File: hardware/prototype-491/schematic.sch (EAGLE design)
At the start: 27 parts, among them IC1 LM2576T, IC2 LM2576T, Q1 220mA/50V/3.5Ω, Q2 220mA/50V/3.5Ω

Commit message: CAM files for PCB
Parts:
- J1: value (none) -> OBD_CONN
- J2: value (none) -> SUPPLY
- JP1: value (none) -> ADXL345
- JP8: value DNP -> UART_CONN
- L1, L2: value (none) -> 100uH
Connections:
- removed net VCC: C2.+, IC2.VIN, J2.1
- net VBAT: now also C2.+, IC2.VIN, J2.1
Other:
- note added: "ECE 491 Group 7 Vehicle Immobilizer Prototype Board Schematic"
- note removed: "ADXL345 Breakout Board"
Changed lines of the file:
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@@
 <clearance class="0" value="0.3048"/>
+</class>
+<class number="1" name="power" width="1.27" drill="0.508">
+<clearance class="1" value="0.508"/>
 </class>
 </classes>
 <parts>
-<part name="JP1" library="microbuilder" deviceset="HEADER-1X9" device="70MIL"/>
+<part name="JP1" library="microbuilder" deviceset="HEADER-1X9" device="70MIL" value="ADXL345"/>
 <part name="U$6" library="microbuilder" deviceset="GND" device=""/>
 <part name="P+1" library="supply1" library_urn="urn:adsk.eagle:library:371" deviceset="+5V" device=""/>
@@
 <part name="GND4" library="supply1" library_urn="urn:adsk.eagle:library:371" deviceset="GND" device=""/>
 <part name="P+2" library="supply1" library_urn="urn:adsk.eagle:library:371" deviceset="+5V" device=""/>
-<part name="JP8" library="SparkFun" deviceset="FTDI_BASIC" device="PTH" value="DNP"/>
+<part name="JP8" library="SparkFun" deviceset="FTDI_BASIC" device="PTH" value="UART_CONN"/>
 <part name="GND32" library="SparkFun" deviceset="GND" device=""/>
 <part name="MCU" library="RPI-Zero" deviceset="RPI-ZERO" device=""/>
@@
 <part name="IC2" library="v-reg-3" deviceset="LM2576" device="T"/>
 <part name="D1" library="1N5822" deviceset="1N5822" device=""/>
-<part name="L1" library="PowerMagnetics" deviceset="WE-TI_1014" device="" technology="_7447480101"/>
+<part name="L1" library="PowerMagnetics" deviceset="WE-TI_1014" device="" technology="_7447480101" value="100uH"/>
 <part name="C1" library="cap-pan40" deviceset="C-PR" device="-3,5X8" value="1000uF"/>
 <part name="C2" library="cap-pan40" deviceset="C-PR" device="-3,5X8" value="100uF"/>
@@
 <part name="IC1" library="v-reg-3" deviceset="LM2576" device="T"/>
 <part name="D2" library="1N5822" deviceset="1N5822" device=""/>
-<part name="L2" library="PowerMagnetics" deviceset="WE-TI_1014" device="" technology="_7447480101"/>
+<part name="L2" library="PowerMagnetics" deviceset="WE-TI_1014" device="" technology="_7447480101" value="100uH"/>
 <part name="C3" library="cap-pan40" deviceset="C-PR" device="-3,5X8" value="1000uF"/>
 <part name="C4" library="cap-pan40" deviceset="C-PR" device="-3,5X8" value="100uF"/>
 <part name="P+7" library="supply1" library_urn="urn:adsk.eagle:library:371" deviceset="+5V" device=""/>
-<part name="SUPPLY1" library="SparkFun-PowerSymbols" deviceset="3.3V" device=""/>
 <part name="SUPPLY4" library="SparkFun-PowerSymbols" deviceset="3.3V" device=""/>
-<part name="FRAME1" library="frames" library_urn="urn:adsk.eagle:library:229" deviceset="FRAME_A_L" device=""/>
-<part name="J1" library="SparkFun-Connectors" deviceset="CONN_08" device="&quot;"/>
-<part name="J2" library="SparkFun-Connectors" deviceset="CONN_02" device="POLAR"/>
+<part name="FRAME1" library="frames" library_urn="urn:adsk.eagle:library:229" deviceset="FRAME_A_L" device="" value="frame"/>
+<part name="J1" library="SparkFun-Connectors" deviceset="CONN_08" device="&quot;" value="OBD_CONN"/>
+<part name="J2" library="SparkFun-Connectors" deviceset="CONN_02" device="POLAR" value="SUPPLY"/>
 <part name="P+8" library="SparkFun" deviceset="VCC" device="" value="VBAT"/>
 <part name="GND9" library="SparkFun" deviceset="GND" device=""/>
@@
 <sheet>
 <plain>
-<text x="294.64" y="71.12" size="1.778" layer="91" rot="R90">ADXL345 Breakout Board
-</text>
+<text x="231.14" y="53.34" size="2.1844" layer="94">ECE 491 Group 7 Vehicle Immobilizer Prototype Board Schematic</text>
 </plain>
 <instances>
@@
 <attribute name="VALUE" x="185.42" y="198.12" size="1.778" layer="96" rot="R180"/>
 </instance>
-<instance part="SUPPLY1" gate="G$1" x="182.88" y="134.62" smashed="yes">
-<attribute name="VALUE" x="180.34" y="139.446" size="1.778" layer="96" rot="R180" align="bottom-center"/>
-</instance>
 <instance part="SUPPLY4" gate="G$1" x="271.78" y="187.96" smashed="yes">
 <attribute name="VALUE" x="269.24" y="192.786" size="1.778" layer="96" rot="R180" align="bottom-center"/>
@@
 </busses>
 <nets>
-<net name="GND" class="0">
+<net name="GND" class="1">
 <segment>
 <pinref part="JP1" gate="A" pin="3"/>
@@
 </segment>
 </net>
-<net name="+5V" class="0">
+<net name="+5V" class="1">
 <segment>
 <wire x1="147.32" y1="127" x2="147.32" y2="144.78" width="0.1524" layer="91"/>
@@
 </segment>
 </net>
-<net name="VBAT" class="0">
+<net name="VBAT" class="1">
 <segment>
 <wire x1="254" y1="99.06" x2="254" y2="93.98" width="0.1524" layer="91"/>
@@
 <pinref part="J1" gate="G$1" pin="8"/>
 <wire x1="254" y1="93.98" x2="248.92" y2="93.98" width="0.1524" layer="91"/>
+</segment>
+<segment>
+<wire x1="111.76" y1="182.88" x2="91.44" y2="182.88" width="0.1524" layer="91"/>
+<wire x1="91.44" y1="182.88" x2="83.82" y2="182.88" width="0.1524" layer="91"/>
+<wire x1="83.82" y1="182.88" x2="83.82" y2="193.04" width="0.1524" layer="91"/>
+<pinref part="P+4" gate="1" pin="VCC"/>
+<pinref part="IC2" gate="A" pin="VIN"/>
+<pinref part="C2" gate="G$1" pin="+"/>
+<junction x="91.44" y="182.88"/>
+</segment>
+<segment>
+<pinref part="J2" gate="G$1" pin="1"/>
+<wire x1="279.4" y1="147.32" x2="276.86" y2="147.32" width="0.1524" layer="91"/>
+<wire x1="276.86" y1="147.32" x2="276.86" y2="152.4" width="0.1524" layer="91"/>
+<pinref part="P+8" gate="1" pin="VCC"/>
 </segment>
 </net>
@@
 </segment>
 </net>
-<net name="VCC" class="0">
-<segment>
-<wire x1="111.76" y1="182.88" x2="91.44" y2="182.88" width="0.1524" layer="91"/>
-<wire x1="91.44" y1="182.88" x2="83.82" y2="182.88" width="0.1524" layer="91"/>
-<wire x1="83.82" y1="182.88" x2="83.82" y2="193.04" width="0.1524" layer="91"/>
-<pinref part="P+4" gate="1" pin="VCC"/>
-<pinref part="IC2" gate="A" pin="VIN"/>
-<pinref part="C2" gate="G$1" pin="+"/>
-<junction x="91.44" y="182.88"/>
-</segment>
-<segment>
-<pinref part="J2" gate="G$1" pin="1"/>
-<wire x1="279.4" y1="147.32" x2="276.86" y2="147.32" width="0.1524" layer="91"/>
-<wire x1="276.86" y1="147.32" x2="276.86" y2="152.4" width="0.1524" layer="91"/>
-<pinref part="P+8" gate="1" pin="VCC"/>
-</segment>
-</net>
 <net name="3.3V" class="0">
-<segment>
-<pinref part="R2" gate="G$1" pin="2"/>
-<wire x1="182.88" y1="129.54" x2="182.88" y2="132.08" width="0.1524" layer="91"/>
-<pinref part="SUPPLY2" gate="G$1" pin="3.3V"/>
-<wire x1="182.88" y1="132.08" x2="182.88" y2="134.62" width="0.1524" layer="91"/>
-<wire x1="182.88" y1="132.08" x2="190.5" y2="132.08" width="0.1524" layer="91"/>
-<junction x="182.88" y="132.08"/>
-<pinref part="Q1" gate="NMOS" pin="G"/>
-<wire x1="190.5" y1="132.08" x2="190.5" y2="119.38" width="0.1524" layer="91"/>
-<pinref part="SUPPLY1" gate="G$1" pin="3.3V"/>
-<junction x="182.88" y="134.62"/>
-</segment>
 <segment>
 <pinref part="R4" gate="G$1" pin="2"/>
@@
 <pinref part="SUPPLY4" gate="G$1" pin="3.3V"/>
 </segment>
+<segment>
+<pinref part="R2" gate="G$1" pin="2"/>
+<wire x1="182.88" y1="129.54" x2="182.88" y2="132.08" width="0.1524" layer="91"/>
+<wire x1="182.88" y1="132.08" x2="190.5" y2="132.08" width="0.1524" layer="91"/>
+<pinref part="Q1" gate="NMOS" pin="G"/>
+<wire x1="190.5" y1="132.08" x2="190.5" y2="119.38" width="0.1524" layer="91"/>
+<pinref part="SUPPLY2" gate="G$1" pin="3.3V"/>
+<wire x1="182.88" y1="134.62" x2="182.88" y2="132.08" width="0.1524" layer="91"/>
+<junction x="182.88" y="132.08"/>
+</segment>
 </net>
 <net name="TX_5V" class="0">
@@
 </sheet>
 </sheets>
+<errors>
+</errors>
 </schematic>
 </drawing>
 <compatibility>
-<note version="6.3" minversion="6.2.2" severity="warning">
-Since Version 6.2.2 text objects can contain more than one line,
-which will not be processed correctly with this version.
-</note>
 <note version="8.2" severity="warning">
 Since Version 8.2, EAGLE supports online libraries. The ids

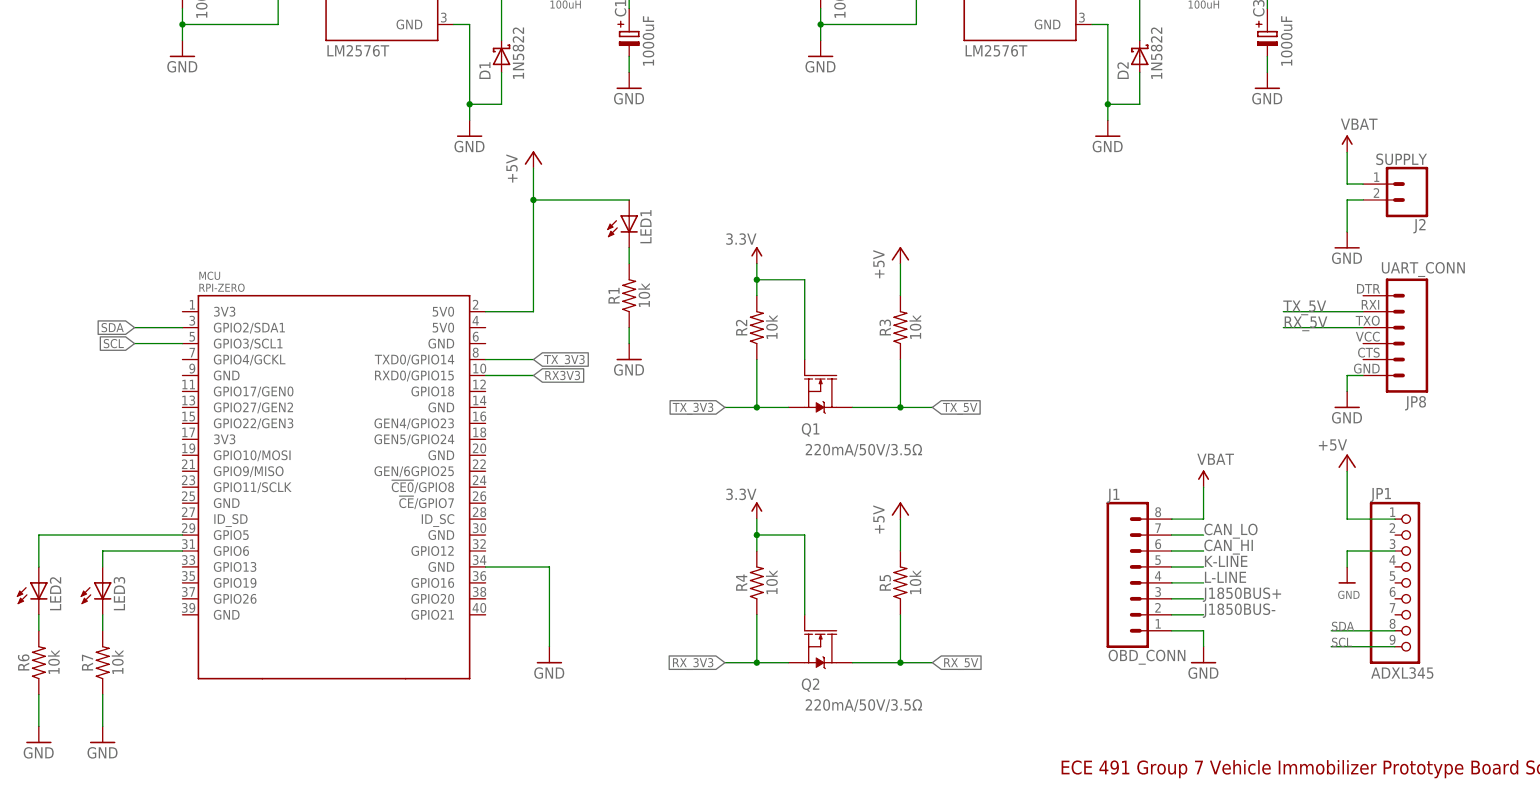
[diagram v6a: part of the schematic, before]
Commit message: android app plus updated board
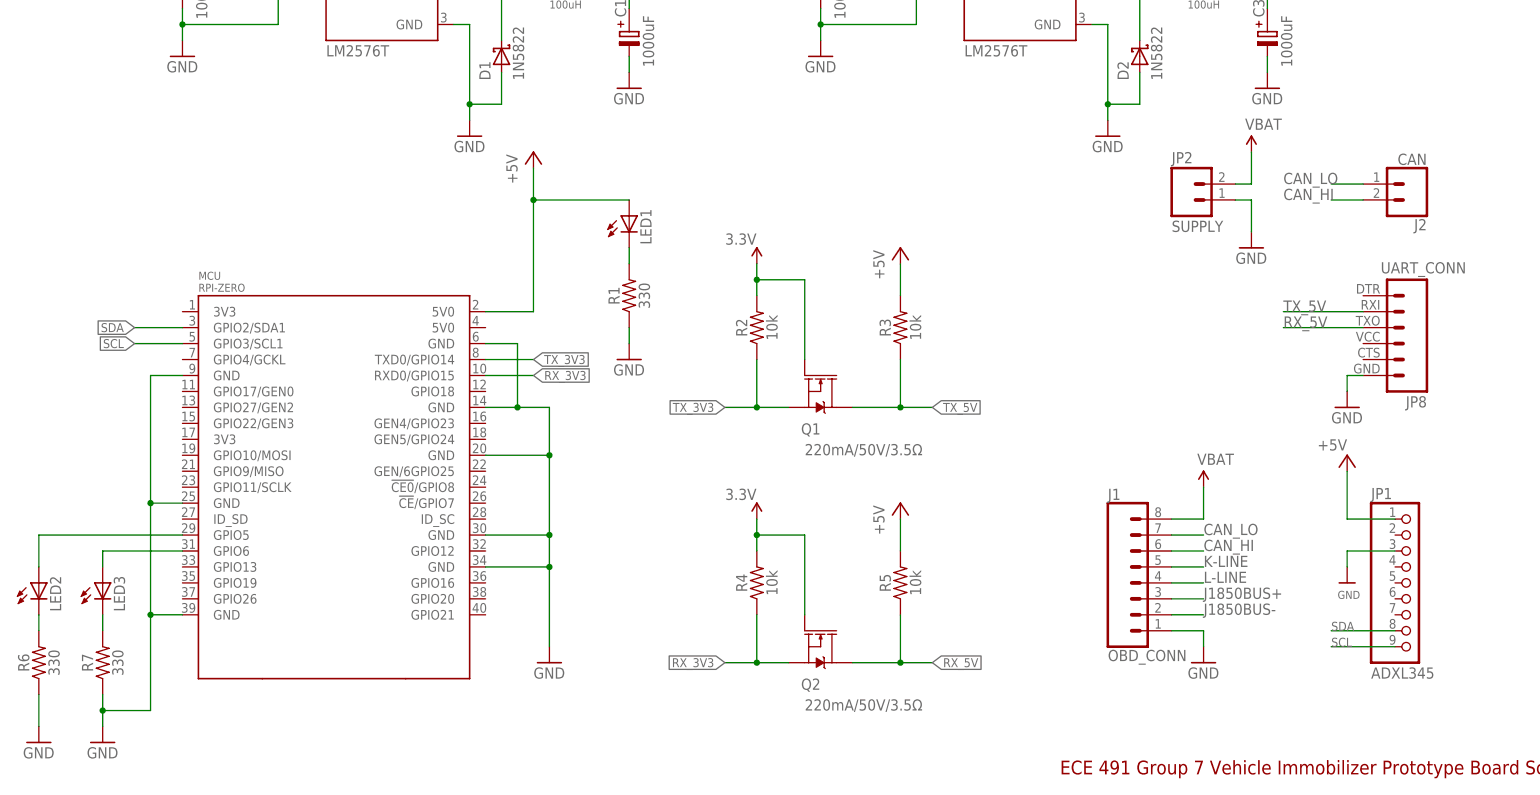
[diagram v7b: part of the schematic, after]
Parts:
- added JP2: SUPPLY, SparkFun:M023.5MM
- J2: value SUPPLY -> CAN
- R1, R6, R7: value 10k -> 330
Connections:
- net N$2 renamed STAT_LED1
- net N$3 renamed STAT_LED2
- removed net RX3V3: MCU.RXD0/GPIO15
- net CAN_HI: now also J2.2
- net CAN_LO: now also J2.1
- net GND: now also JP2.1, MCU.GND@1, MCU.GND@2, MCU.GND@3, MCU.GND@4, MCU.GND@5, MCU.GND@6, MCU.GND@8; no longer J2.2
- net RX_3V3: now also MCU.RXD0/GPIO15
- net VBAT: now also JP2.2; no longer J2.1
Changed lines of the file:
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@@
 <part name="GND32" library="SparkFun" deviceset="GND" device=""/>
 <part name="MCU" library="RPI-Zero" deviceset="RPI-ZERO" device=""/>
-<part name="R1" library="SparkFun-Resistors" deviceset="10KOHM" device="-HORIZ-1/4W-5%" value="10k"/>
+<part name="R1" library="SparkFun-Resistors" deviceset="10KOHM" device="-HORIZ-1/4W-5%" value="330"/>
 <part name="P+30" library="SparkFun" deviceset="VCC" device="" value="VBAT"/>
 <part name="GND13" library="SparkFun" deviceset="GND" device=""/>
@@
 <part name="FRAME1" library="frames" library_urn="urn:adsk.eagle:library:229" deviceset="FRAME_A_L" device="" value="frame"/>
 <part name="J1" library="SparkFun-Connectors" deviceset="CONN_08" device="&quot;" value="OBD_CONN"/>
-<part name="J2" library="SparkFun-Connectors" deviceset="CONN_02" device="POLAR" value="SUPPLY"/>
+<part name="J2" library="SparkFun-Connectors" deviceset="CONN_02" device="POLAR" value="CAN"/>
 <part name="P+8" library="SparkFun" deviceset="VCC" device="" value="VBAT"/>
 <part name="GND9" library="SparkFun" deviceset="GND" device=""/>
 <part name="LED2" library="adafruit" library_urn="urn:adsk.eagle:library:420" deviceset="LED" device="3MM"/>
 <part name="LED3" library="adafruit" library_urn="urn:adsk.eagle:library:420" deviceset="LED" device="3MM"/>
-<part name="R6" library="SparkFun-Resistors" deviceset="10KOHM" device="-HORIZ-1/4W-5%" value="10k"/>
-<part name="R7" library="SparkFun-Resistors" deviceset="10KOHM" device="-HORIZ-1/4W-5%" value="10k"/>
+<part name="R6" library="SparkFun-Resistors" deviceset="10KOHM" device="-HORIZ-1/4W-5%" value="330"/>
+<part name="R7" library="SparkFun-Resistors" deviceset="10KOHM" device="-HORIZ-1/4W-5%" value="330"/>
 <part name="GND10" library="supply1" library_urn="urn:adsk.eagle:library:371" deviceset="GND" device=""/>
 <part name="GND11" library="supply1" library_urn="urn:adsk.eagle:library:371" deviceset="GND" device=""/>
+<part name="JP2" library="SparkFun" deviceset="M02" device="3.5MM" value="SUPPLY"/>
 </parts>
 <sheets>
@@
 <attribute name="NAME" x="289.56" y="141.732" size="1.778" layer="95" font="vector" rot="R180"/>
 </instance>
-<instance part="P+8" gate="1" x="276.86" y="152.4" smashed="yes">
-<attribute name="VALUE" x="275.844" y="155.956" size="1.778" layer="96"/>
-</instance>
-<instance part="GND9" gate="1" x="276.86" y="137.16" smashed="yes">
-<attribute name="VALUE" x="274.32" y="134.62" size="1.778" layer="96"/>
+<instance part="P+8" gate="1" x="261.62" y="152.4" smashed="yes">
+<attribute name="VALUE" x="260.604" y="155.956" size="1.778" layer="96"/>
+</instance>
+<instance part="GND9" gate="1" x="261.62" y="137.16" smashed="yes">
+<attribute name="VALUE" x="259.08" y="134.62" size="1.778" layer="96"/>
 </instance>
 <instance part="LED2" gate="G$1" x="68.58" y="83.82" smashed="yes">
@@
 <instance part="GND11" gate="1" x="78.74" y="58.42" smashed="yes">
 <attribute name="VALUE" x="76.2" y="55.88" size="1.778" layer="96"/>
+</instance>
+<instance part="JP2" gate="G$1" x="251.46" y="144.78" smashed="yes">
+<attribute name="VALUE" x="248.92" y="139.7" size="1.778" layer="96"/>
+<attribute name="NAME" x="248.92" y="150.622" size="1.778" layer="95"/>
 </instance>
 </instances>
@@
 <wire x1="284.48" y1="88.9" x2="276.86" y2="88.9" width="0.1524" layer="91"/>
 <wire x1="276.86" y1="88.9" x2="276.86" y2="86.36" width="0.1524" layer="91"/>
-</segment>
-<segment>
-<wire x1="149.86" y1="86.36" x2="149.86" y2="73.66" width="0.1524" layer="91"/>
-<pinref part="GND1" gate="1" pin="GND"/>
-<pinref part="MCU" gate="G$1" pin="GND@7"/>
-<wire x1="139.7" y1="86.36" x2="149.86" y2="86.36" width="0.1524" layer="91"/>
 </segment>
 <segment>
@@
 </segment>
 <segment>
-<pinref part="J2" gate="G$1" pin="2"/>
-<wire x1="279.4" y1="144.78" x2="276.86" y2="144.78" width="0.1524" layer="91"/>
-<wire x1="276.86" y1="144.78" x2="276.86" y2="139.7" width="0.1524" layer="91"/>
+<wire x1="261.62" y1="144.78" x2="261.62" y2="139.7" width="0.1524" layer="91"/>
 <pinref part="GND9" gate="1" pin="GND"/>
+<pinref part="JP2" gate="G$1" pin="1"/>
+<wire x1="259.08" y1="144.78" x2="261.62" y2="144.78" width="0.1524" layer="91"/>
 </segment>
 <segment>
@@
 </segment>
 <segment>
+<pinref part="MCU" gate="G$1" pin="GND@8"/>
+<wire x1="139.7" y1="121.92" x2="144.78" y2="121.92" width="0.1524" layer="91"/>
+<pinref part="MCU" gate="G$1" pin="GND@4"/>
+<wire x1="139.7" y1="111.76" x2="144.78" y2="111.76" width="0.1524" layer="91"/>
+<pinref part="MCU" gate="G$1" pin="GND@5"/>
+<wire x1="144.78" y1="111.76" x2="149.86" y2="111.76" width="0.1524" layer="91"/>
+<wire x1="139.7" y1="104.14" x2="149.86" y2="104.14" width="0.1524" layer="91"/>
+<pinref part="MCU" gate="G$1" pin="GND@6"/>
+<wire x1="139.7" y1="91.44" x2="149.86" y2="91.44" width="0.1524" layer="91"/>
+<wire x1="149.86" y1="86.36" x2="149.86" y2="73.66" width="0.1524" layer="91"/>
+<pinref part="GND1" gate="1" pin="GND"/>
+<pinref part="MCU" gate="G$1" pin="GND@7"/>
+<wire x1="139.7" y1="86.36" x2="149.86" y2="86.36" width="0.1524" layer="91"/>
+<wire x1="149.86" y1="91.44" x2="149.86" y2="86.36" width="0.1524" layer="91"/>
+<junction x="149.86" y="86.36"/>
+<wire x1="149.86" y1="104.14" x2="149.86" y2="91.44" width="0.1524" layer="91"/>
+<junction x="149.86" y="91.44"/>
+<wire x1="149.86" y1="111.76" x2="149.86" y2="104.14" width="0.1524" layer="91"/>
+<junction x="149.86" y="104.14"/>
+<wire x1="144.78" y1="121.92" x2="144.78" y2="111.76" width="0.1524" layer="91"/>
+<junction x="144.78" y="111.76"/>
+</segment>
+<segment>
+<pinref part="MCU" gate="G$1" pin="GND@1"/>
+<wire x1="91.44" y1="116.84" x2="86.36" y2="116.84" width="0.1524" layer="91"/>
+<pinref part="MCU" gate="G$1" pin="GND@2"/>
+<wire x1="91.44" y1="96.52" x2="86.36" y2="96.52" width="0.1524" layer="91"/>
+<pinref part="MCU" gate="G$1" pin="GND@3"/>
+<wire x1="91.44" y1="78.74" x2="86.36" y2="78.74" width="0.1524" layer="91"/>
 <pinref part="R7" gate="G$1" pin="1"/>
-<wire x1="78.74" y1="66.04" x2="78.74" y2="60.96" width="0.1524" layer="91"/>
+<wire x1="78.74" y1="66.04" x2="78.74" y2="63.5" width="0.1524" layer="91"/>
 <pinref part="GND11" gate="1" pin="GND"/>
+<wire x1="78.74" y1="63.5" x2="78.74" y2="60.96" width="0.1524" layer="91"/>
+<wire x1="86.36" y1="78.74" x2="86.36" y2="63.5" width="0.1524" layer="91"/>
+<wire x1="86.36" y1="63.5" x2="78.74" y2="63.5" width="0.1524" layer="91"/>
+<junction x="78.74" y="63.5"/>
+<wire x1="86.36" y1="96.52" x2="86.36" y2="78.74" width="0.1524" layer="91"/>
+<junction x="86.36" y="78.74"/>
+<wire x1="86.36" y1="116.84" x2="86.36" y2="96.52" width="0.1524" layer="91"/>
+<junction x="86.36" y="96.52"/>
 </segment>
 </net>
@@
 </segment>
 </net>
-<net name="RX3V3" class="0">
-<segment>
-<pinref part="MCU" gate="G$1" pin="RXD0/GPIO15"/>
-<wire x1="139.7" y1="116.84" x2="147.32" y2="116.84" width="0.1524" layer="91"/>
-<label x="147.32" y="116.84" size="1.4224" layer="95" xref="yes"/>
-</segment>
-</net>
 <net name="SDA" class="0">
 <segment>
@@
 <wire x1="254" y1="88.9" x2="248.92" y2="88.9" width="0.1524" layer="91"/>
 </segment>
+<segment>
+<pinref part="J2" gate="G$1" pin="2"/>
+<wire x1="279.4" y1="144.78" x2="274.32" y2="144.78" width="0.1524" layer="91"/>
+<label x="266.7" y="144.78" size="1.778" layer="95"/>
+</segment>
 </net>
 <net name="CAN_LO" class="0">
@@
 <pinref part="J1" gate="G$1" pin="7"/>
 <wire x1="254" y1="91.44" x2="248.92" y2="91.44" width="0.1524" layer="91"/>
+</segment>
+<segment>
+<pinref part="J2" gate="G$1" pin="1"/>
+<wire x1="279.4" y1="147.32" x2="274.32" y2="147.32" width="0.1524" layer="91"/>
+<label x="266.7" y="147.32" size="1.778" layer="95"/>
 </segment>
 </net>
@@
 </segment>
 <segment>
-<pinref part="J2" gate="G$1" pin="1"/>
-<wire x1="279.4" y1="147.32" x2="276.86" y2="147.32" width="0.1524" layer="91"/>
-<wire x1="276.86" y1="147.32" x2="276.86" y2="152.4" width="0.1524" layer="91"/>
+<wire x1="261.62" y1="147.32" x2="261.62" y2="152.4" width="0.1524" layer="91"/>
 <pinref part="P+8" gate="1" pin="VCC"/>
+<pinref part="JP2" gate="G$1" pin="2"/>
+<wire x1="259.08" y1="147.32" x2="261.62" y2="147.32" width="0.1524" layer="91"/>
 </segment>
 </net>
@@
 <label x="177.8" y="71.12" size="1.4224" layer="95" rot="R180" xref="yes"/>
 </segment>
+<segment>
+<pinref part="MCU" gate="G$1" pin="RXD0/GPIO15"/>
+<wire x1="139.7" y1="116.84" x2="147.32" y2="116.84" width="0.1524" layer="91"/>
+<label x="147.32" y="116.84" size="1.4224" layer="95" xref="yes"/>
+</segment>
 </net>
 <net name="N$1" class="0">
@@
 </segment>
 </net>
-<net name="N$2" class="0">
+<net name="STAT_LED1" class="0">
 <segment>
 <pinref part="MCU" gate="G$1" pin="GPIO5"/>
@@
 </segment>
 </net>
-<net name="N$3" class="0">
+<net name="STAT_LED2" class="0">
 <segment>
 <pinref part="MCU" gate="G$1" pin="GPIO6"/>
